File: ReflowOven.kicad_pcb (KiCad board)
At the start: 2 copper layers, 54.5 x 104.5 mm, 17 parts, among them J1 Conn_01x20_MountingPin, J2 Conn_01x20_MountingPin, J3 Conn_01x05, J4 Conn_01x04, J5 Conn_01x02, J6 Conn_01x02, J7 Screw_Terminal_01x02, J8 Conn_01x02, J9 Conn_01x02

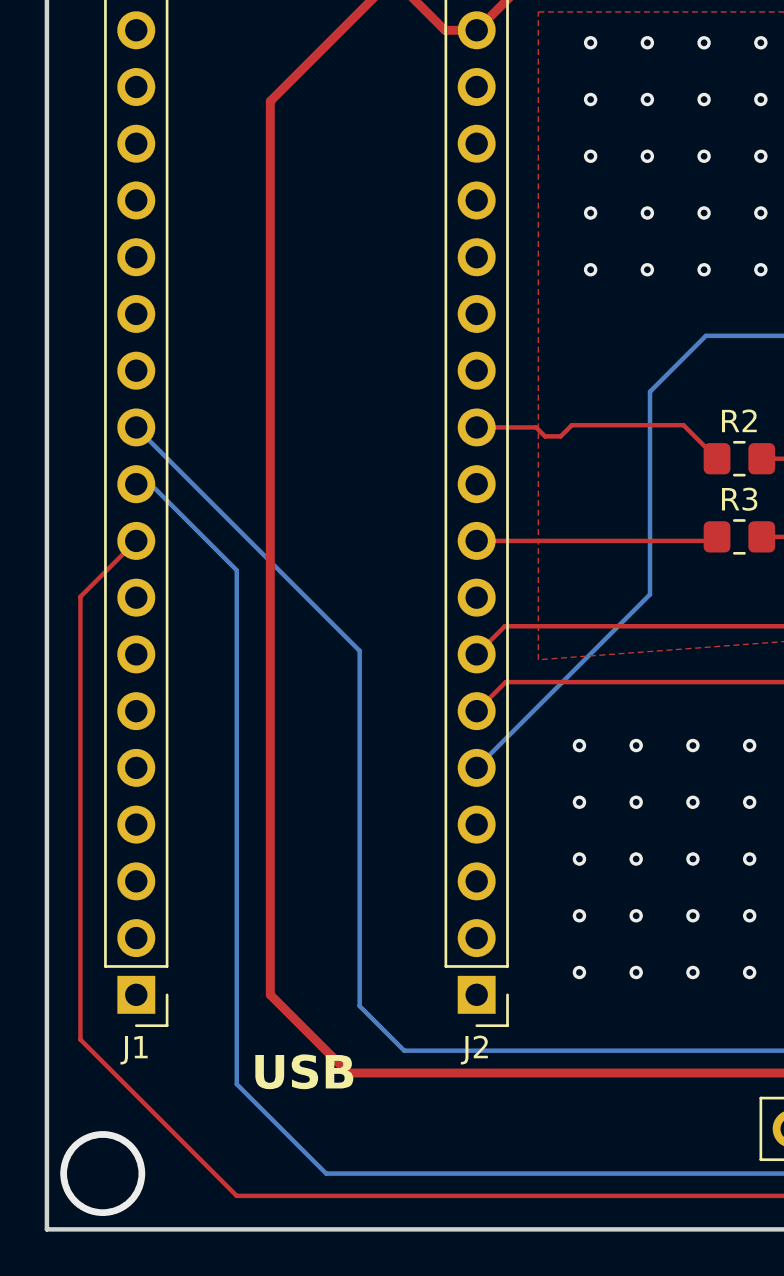
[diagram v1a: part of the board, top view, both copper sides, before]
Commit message: SPI Lines updates
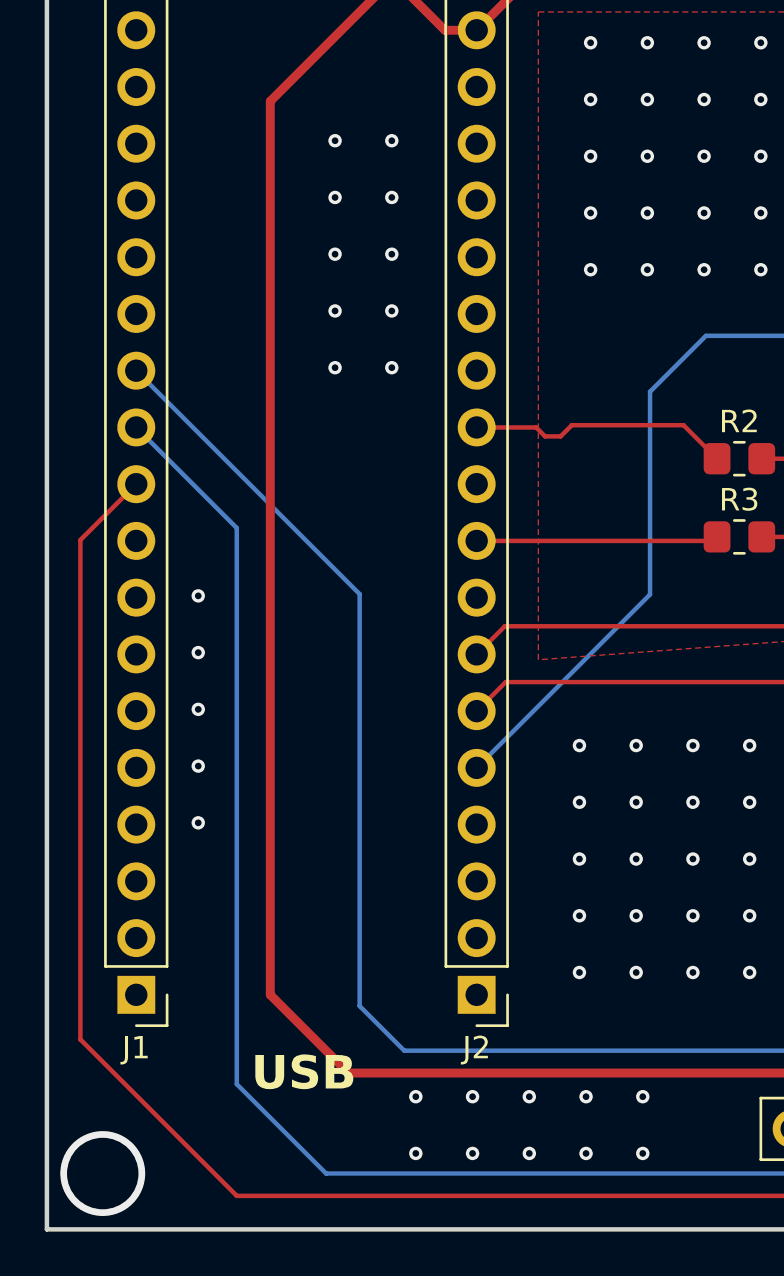
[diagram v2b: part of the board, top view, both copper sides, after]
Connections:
- J1 pad 10: SCK -> DO
- J1 pad 11: CS -> SCK
- J1 pad 12: unconnected-(J1-Pin_12-Pad12) -> CS
- J1 pad 9: DO -> unconnected-(J1-Pin_9-Pad9)
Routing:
- net DO: track 69.5 -> 72.7 mm
- net CS: track 59.3 -> 61.8 mm
- net SCK: track 62.4 -> 64.6 mm
- net GND: vias 105 -> 130
